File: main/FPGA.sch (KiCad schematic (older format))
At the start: 27 parts

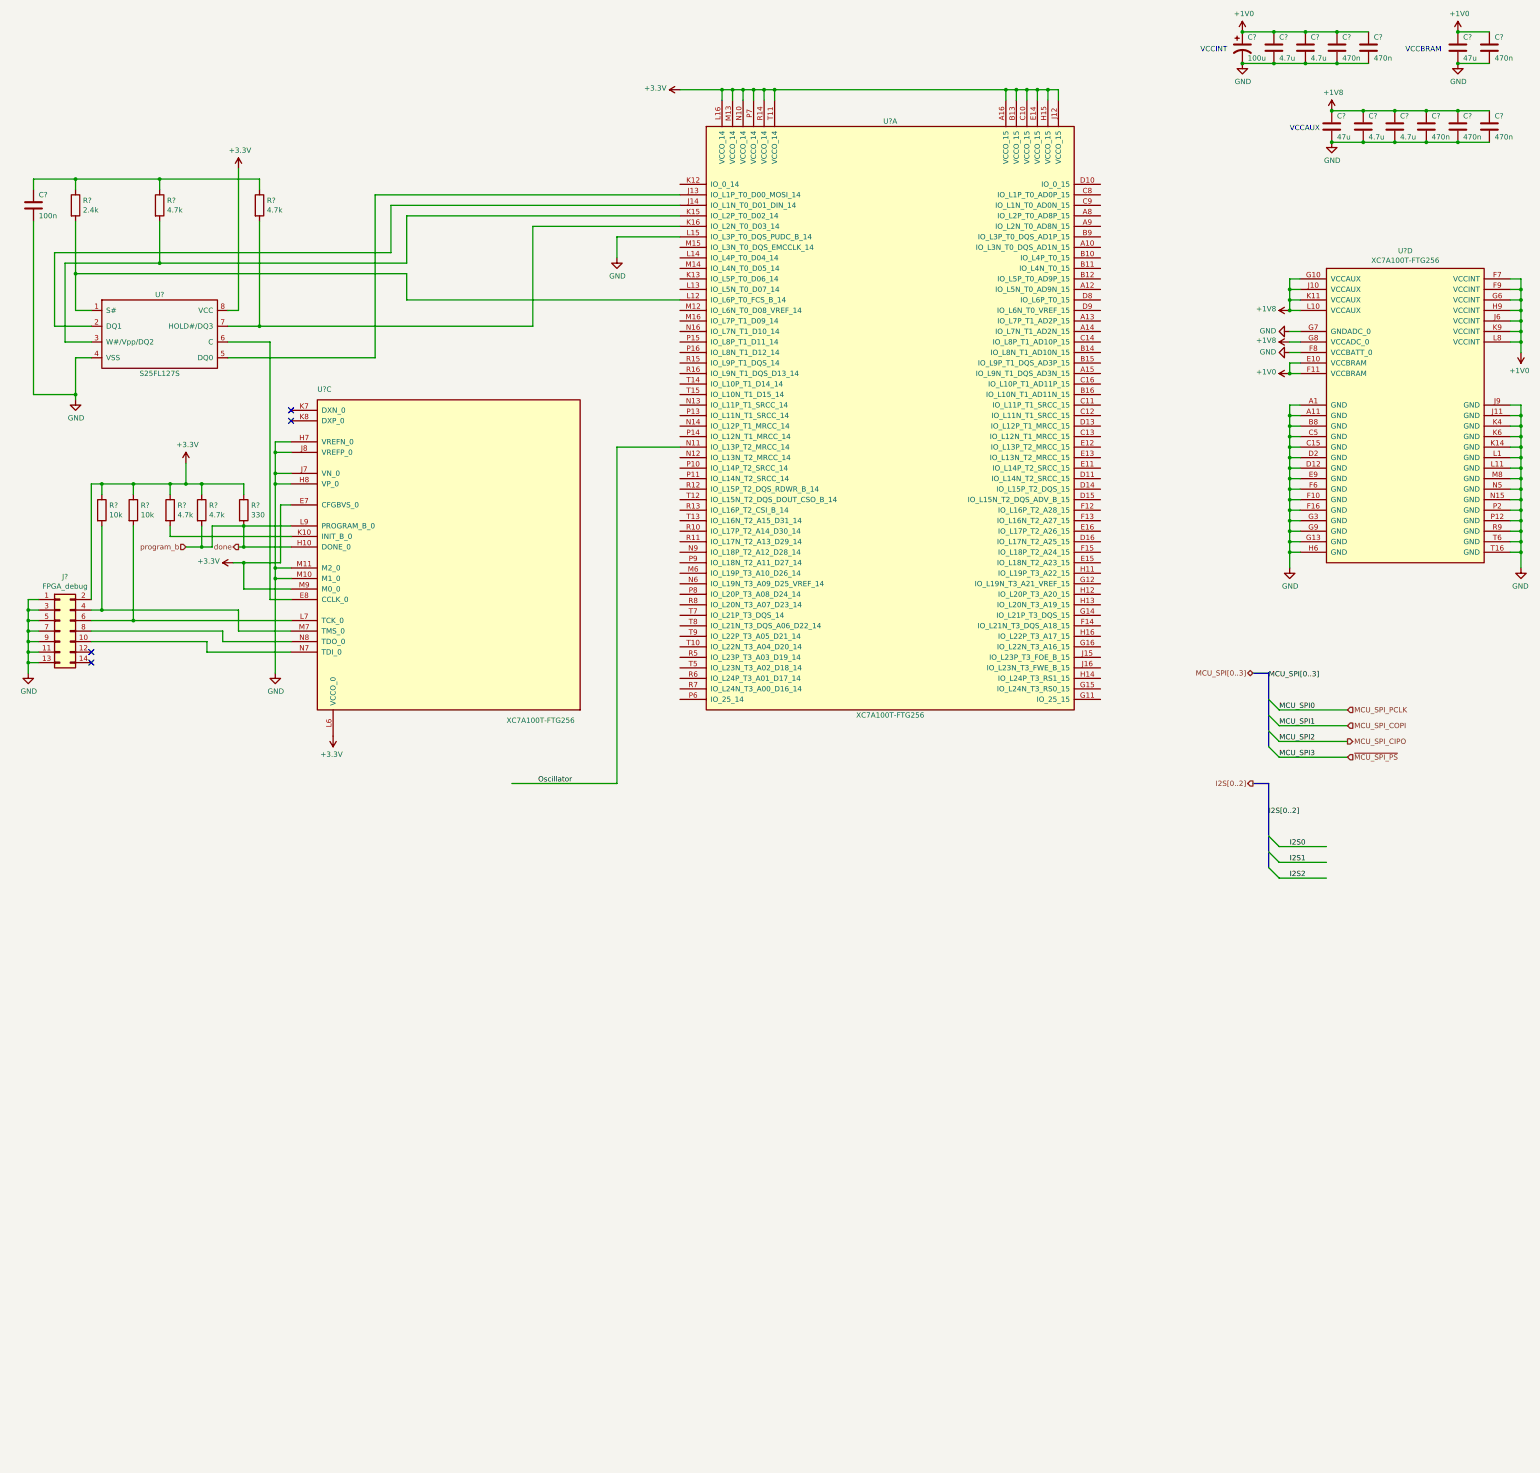
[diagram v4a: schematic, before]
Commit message: Finish (?) setting up FPGA as in the slides
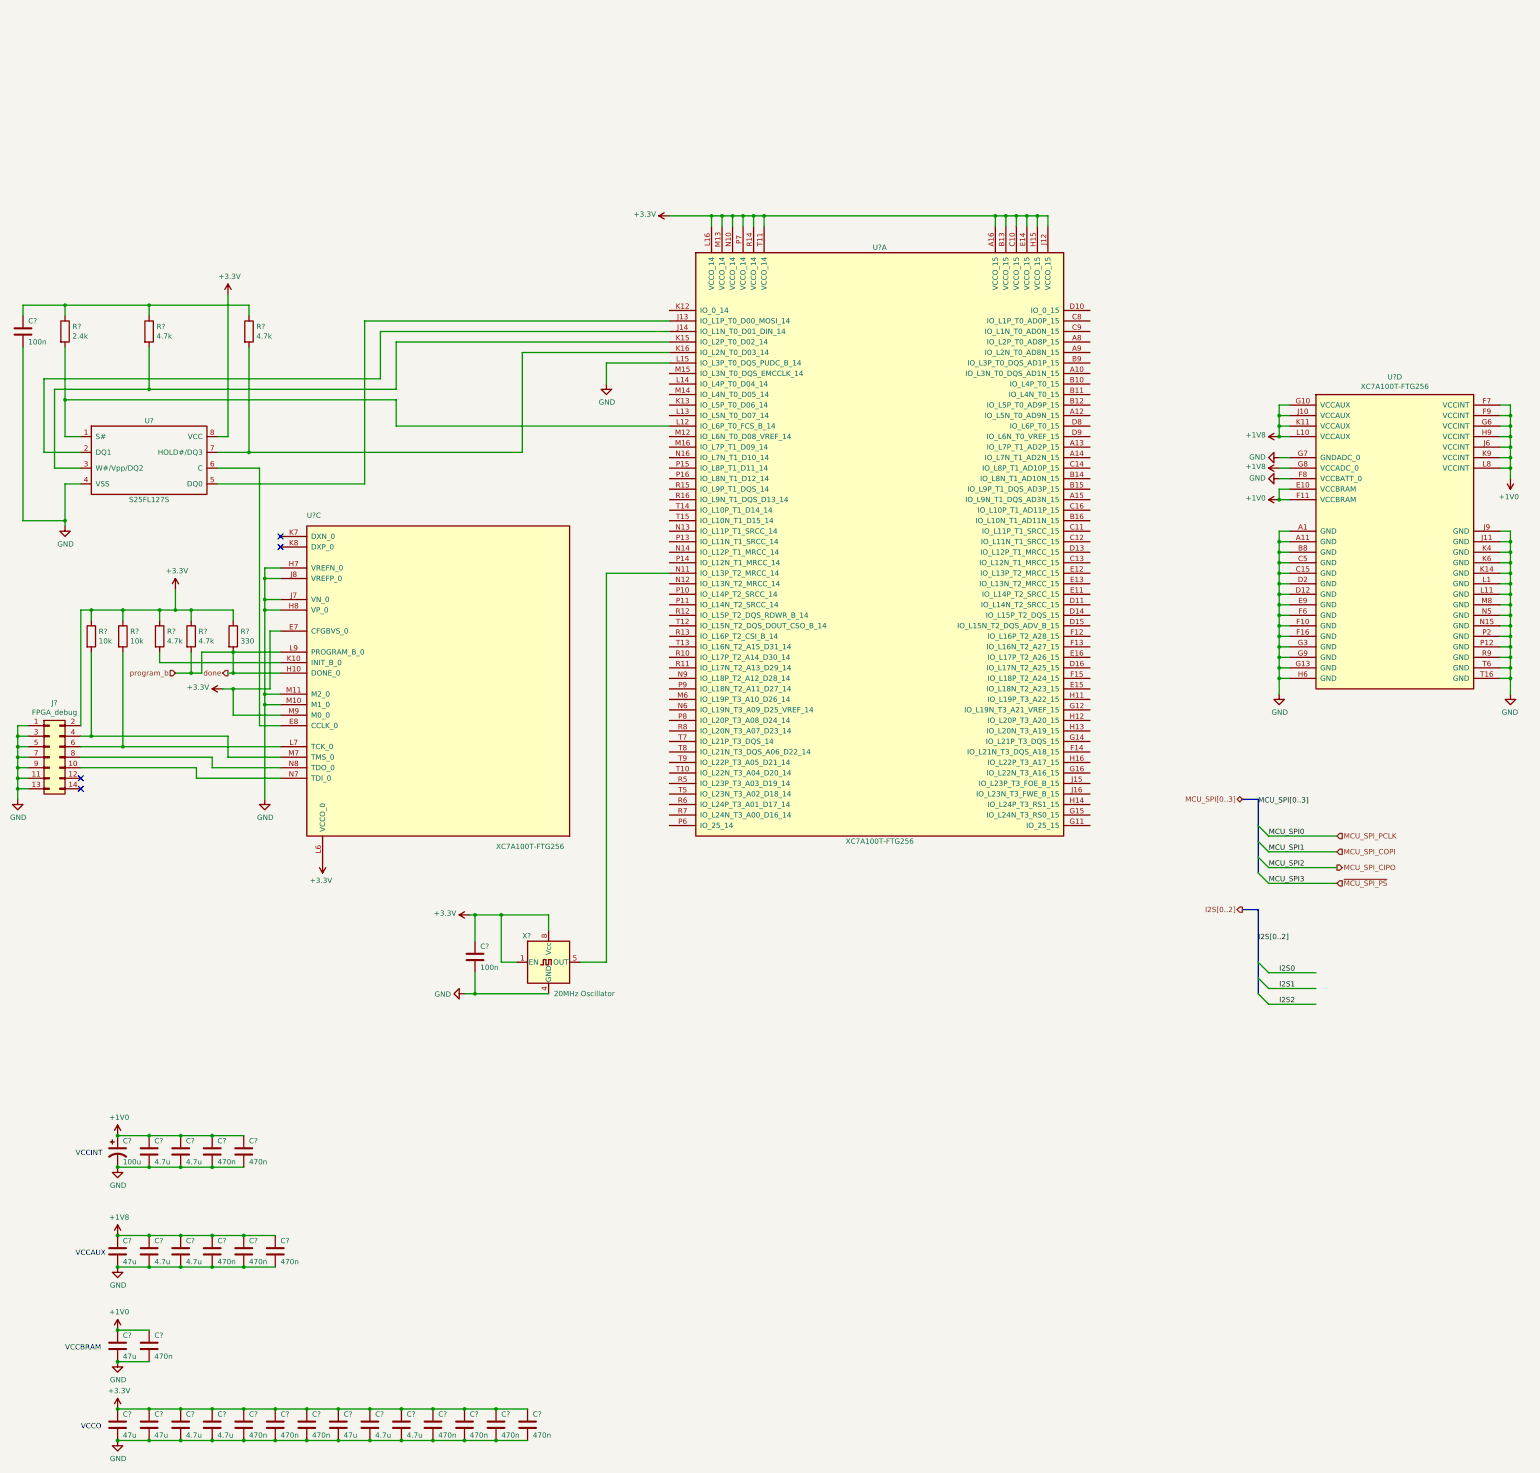
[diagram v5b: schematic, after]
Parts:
- added C?: 100n, symbol Device:C
- added C? (x3): 47u, symbol Device:C
- added C? (x4): 4.7u, symbol Device:C
- added C? (x7): 470n, symbol Device:C
- added X?: 20MHz Oscillator, Oscillator:Oscillator_DIP-8, symbol Oscillator:CXO_DIP8
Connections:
- net +3V3: now also C?.1, C?.1, C?.1, C?.1, C?.1, C?.1, C?.1, C?.1, C?.1, C?.1, C?.1, C?.1, C?.1, C?.1, C?.1, X?.1 (EN), X?.8 (Vcc)
- net GND: now also C?.2, C?.2, C?.2, C?.2, C?.2, C?.2, C?.2, C?.2, C?.2, C?.2, C?.2, C?.2, C?.2, C?.2, C?.2, X?.4 (GND)
- net Oscillator: no longer names the net of U?.N11 (IO_L13P_T2_MRCC_14)
- net Oscillator: now also X?.5 (OUT)
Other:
- note added: "VCCO"
- moved on the sheet: C?, J?, R?, U?, U?A, U?C, U?D

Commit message: Add FPGA oscillator, cleanup
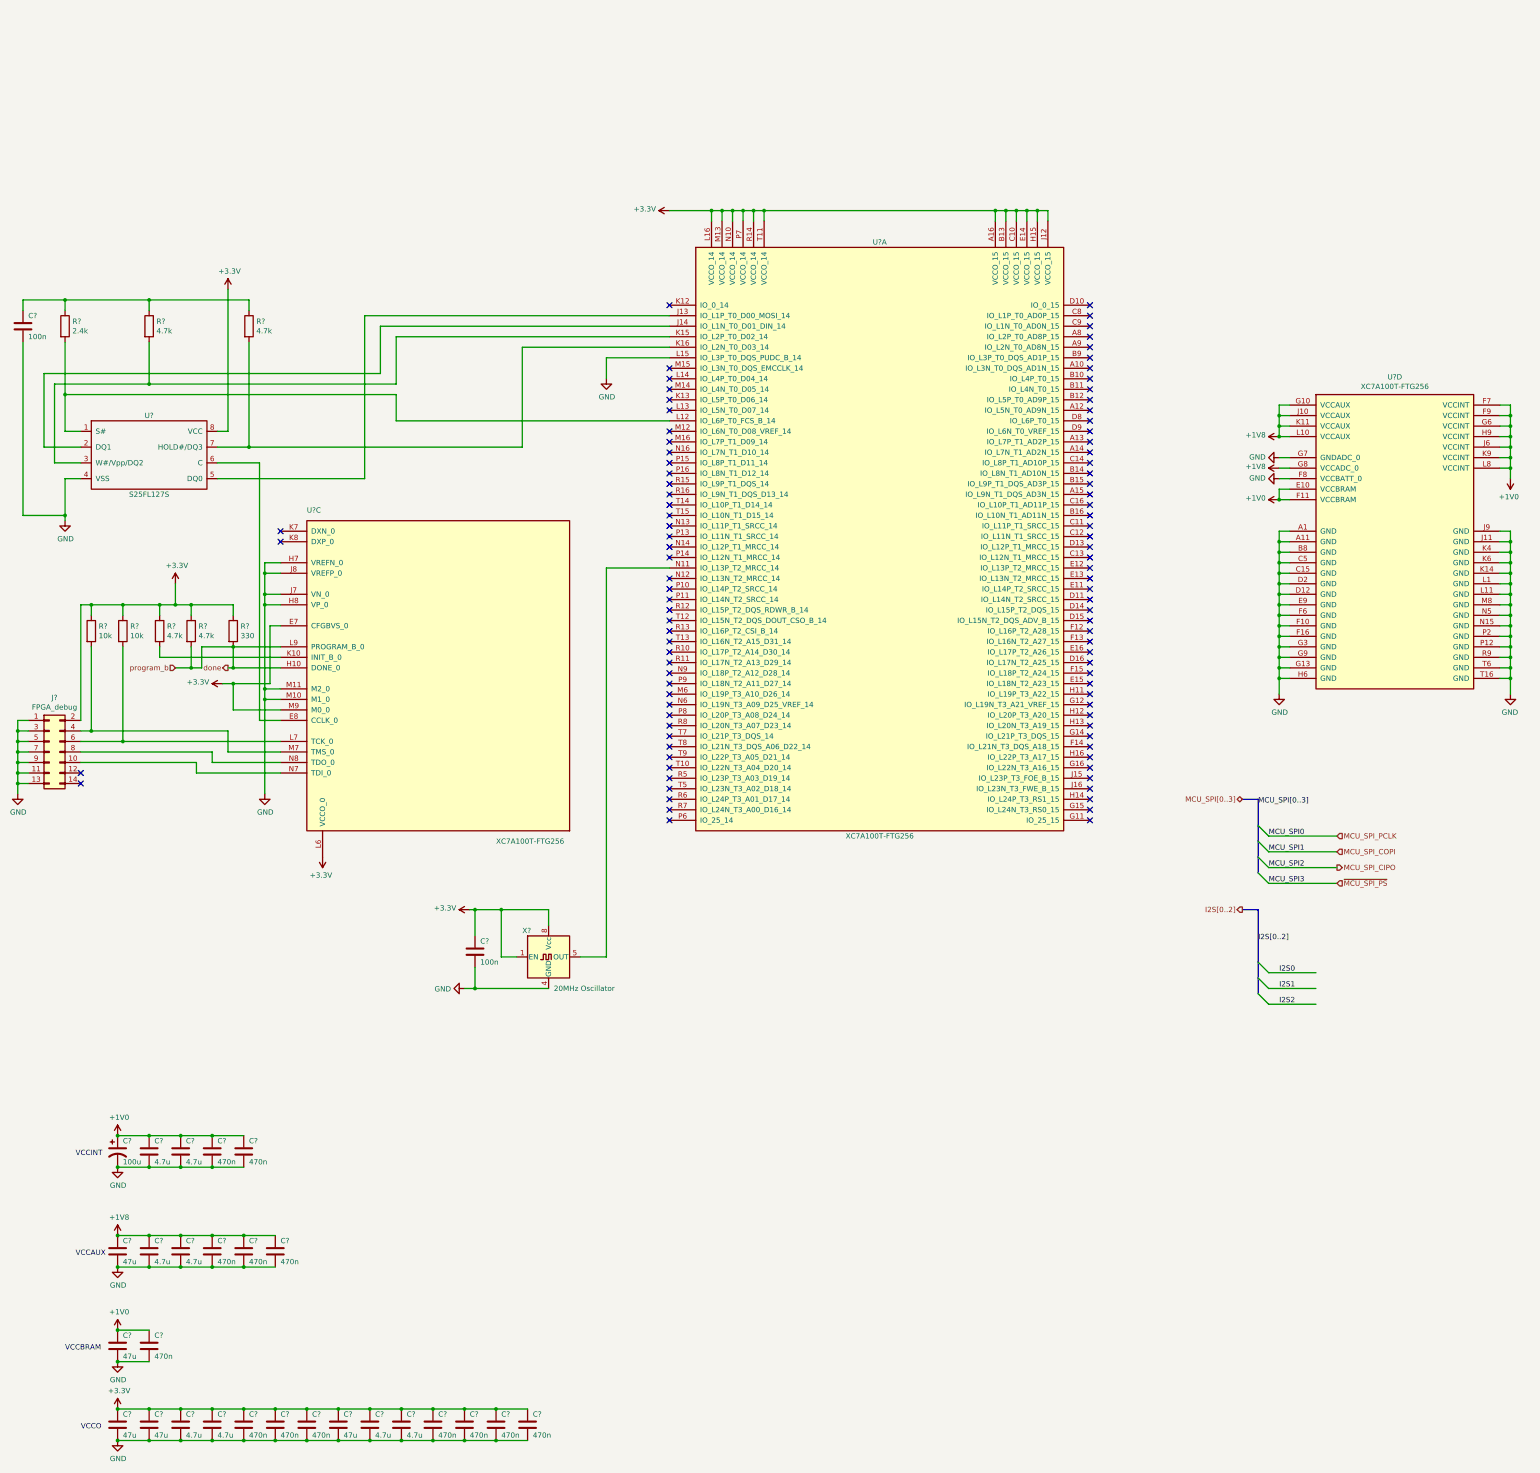
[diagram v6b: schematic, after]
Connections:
- no-connect marks 4 -> 97
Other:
- moved on the sheet: C?, J?, R?, U?, U?A, U?C, X?
